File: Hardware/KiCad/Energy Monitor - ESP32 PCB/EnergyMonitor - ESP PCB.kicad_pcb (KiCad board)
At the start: 2 copper layers, 16 parts, among them J1 Conn_02x05_Odd_Even, J2 Conn_02x07_Odd_Even, J3 Conn_02x07_Odd_Even, J4 Conn_02x07_Odd_Even, J5 Conn_02x07_Odd_Even, J6 Conn_02x07_Odd_Even, J7 Conn_02x07_Odd_Even, U1 4072, U2 4072, U3 4072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

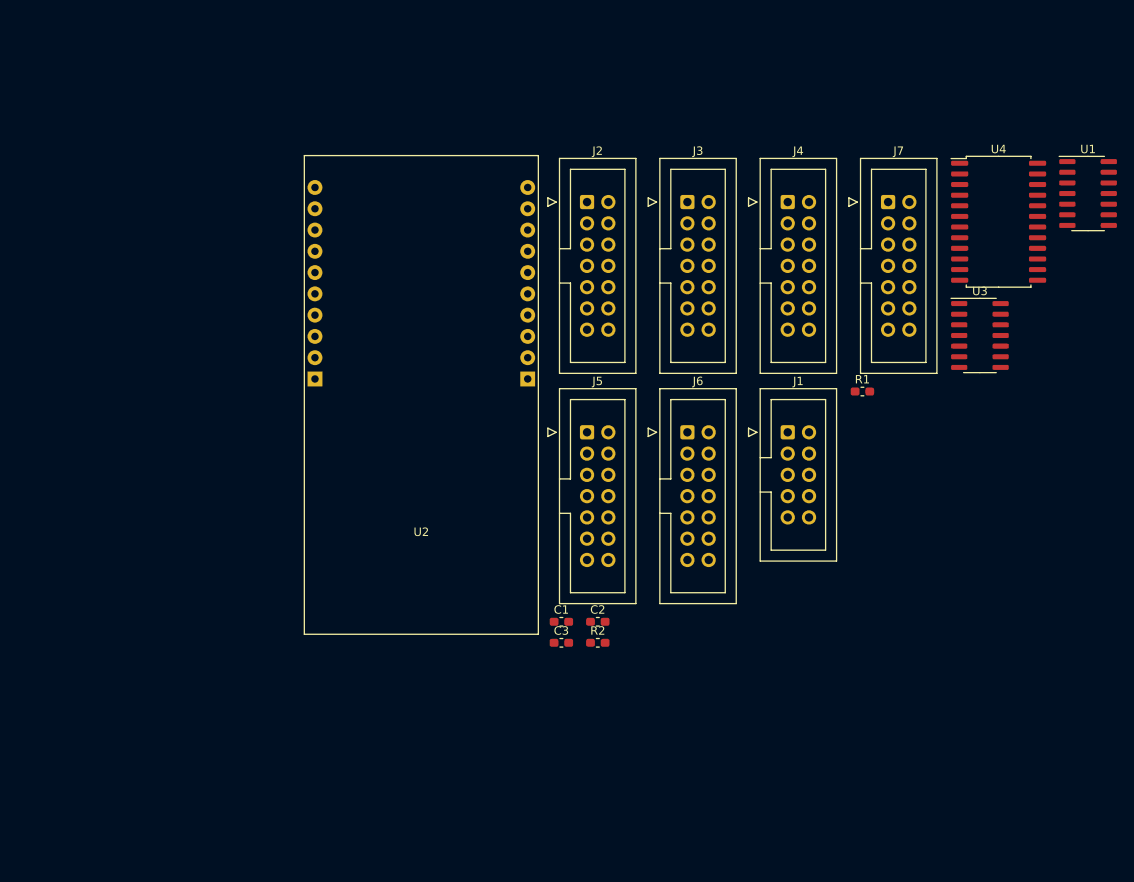
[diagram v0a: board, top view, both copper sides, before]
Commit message: This seems to be getting progressively more complicated. Library cleanup, moved everything to my system library.
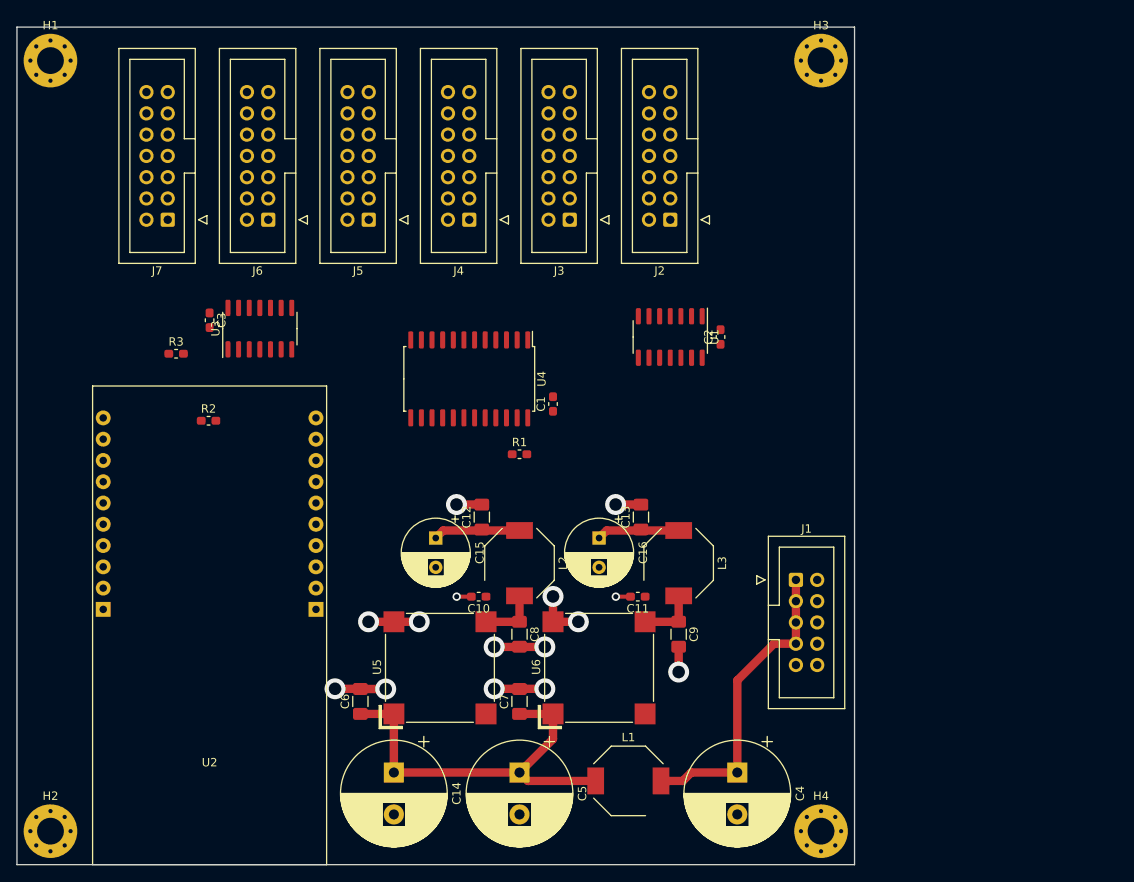
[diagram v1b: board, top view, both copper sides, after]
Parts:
- added C10: 0.1 uF, Capacitor_SMD:C_0603_1608Metric_Pad1.05x0.95mm_HandSolder, F.Cu at (95.1, 108.0)
- added C11: 0.1 uF, Capacitor_SMD:C_0603_1608Metric_Pad1.05x0.95mm_HandSolder, F.Cu at (114.1, 108.0)
- added C12: 22 uF, Capacitor_SMD:C_1206_3216Metric_Pad1.42x1.75mm_HandSolder, F.Cu at (95.5, 98.5)
- added C13: 22 uF, Capacitor_SMD:C_1206_3216Metric_Pad1.42x1.75mm_HandSolder, F.Cu at (114.5, 98.5)
- added C14: CP1, Capacitor_THT:CP_Radial_D12.5mm_P5.00mm, F.Cu at (85.0, 129.0)
- added C15: CP1, Capacitor_THT:CP_Radial_D8.0mm_P3.50mm, F.Cu at (90.0, 101.0)
- added C16: CP1, Capacitor_THT:CP_Radial_D8.0mm_P3.50mm, F.Cu at (109.5, 101.0)
- added C4: CP1, Capacitor_THT:CP_Radial_D12.5mm_P5.00mm, F.Cu at (126.0, 129.0)
- added C5: CP1, Capacitor_THT:CP_Radial_D12.5mm_P5.00mm, F.Cu at (100.0, 129.0)
- added C6: 10 uF, 35V, Capacitor_SMD:C_1206_3216Metric_Pad1.42x1.75mm_HandSolder, F.Cu at (81.0, 120.5)
- added C7: 10 uF, 35V, Capacitor_SMD:C_1206_3216Metric_Pad1.42x1.75mm_HandSolder, F.Cu at (100.0, 120.5)
- added C8: 22 uF, Capacitor_SMD:C_1206_3216Metric_Pad1.42x1.75mm_HandSolder, F.Cu at (100.0, 112.5)
- added C9: 22 uF, Capacitor_SMD:C_1206_3216Metric_Pad1.42x1.75mm_HandSolder, F.Cu at (119.0, 112.5)
- added H1: MountingHole, MountingHole:MountingHole_3.2mm_M3_Pad_Via, F.Cu at (44.0, 44.0)
- added H2: MountingHole, MountingHole:MountingHole_3.2mm_M3_Pad_Via, F.Cu at (44.0, 136.0)
- added H3: MountingHole, MountingHole:MountingHole_3.2mm_M3_Pad_Via, F.Cu at (136.0, 44.0)
- added H4: MountingHole, MountingHole:MountingHole_3.2mm_M3_Pad_Via, F.Cu at (136.0, 136.0)
- added L1: 47 uH, Inductor_SMD:L_Bourns-SRU8028_8.0x8.0mm, F.Cu at (113.0, 130.0)
- added L2: 47 uH, Inductor_SMD:L_Bourns-SRU8028_8.0x8.0mm, F.Cu at (100.0, 104.0)
- added L3: 47 uH, Inductor_SMD:L_Bourns-SRU8028_8.0x8.0mm, F.Cu at (119.0, 104.0)
- added R3: 330R, Resistor_SMD:R_0603_1608Metric_Pad1.05x0.95mm_HandSolder, F.Cu at (59.0, 79.0)
- added U5: VXO7805-500-M, custom:VXO78x-500-M, F.Cu at (90.5, 116.5)
- added U6: VXO7803-500-M, custom:VXO78x-500-M, F.Cu at (109.5, 116.5)
- U2: value 4072 -> ESP32-POE Module
- moved J7 86.0 mm to (58.0, 63.0), turned to 180 degrees
- moved U3 86.0 mm to (69.0, 76.0), turned to 90 degrees
- moved U4 65.9 mm to (94.0, 82.0), turned to 270 degrees
- moved C3 57.0 mm to (63.0, 75.0), turned to 270 degrees
- moved J6 56.1 mm to (70.0, 63.0), turned to 180 degrees
- moved R2 53.5 mm to (62.9, 87.0)
- moved U1 52.7 mm to (118.0, 77.0), turned to 270 degrees
- moved R1 41.6 mm to (100.0, 91.0)
- moved J4 38.1 mm to (94.0, 63.0), turned to 180 degrees
- moved U2 37.4 mm to (63.0, 140.0)
- moved C2 37.0 mm to (124.0, 77.0), turned to 90 degrees
- moved J5 36.4 mm to (82.0, 63.0), turned to 180 degrees
- moved C1 26.0 mm to (104.0, 85.0), turned to 90 degrees
- moved J1 17.6 mm to (133.0, 106.0)
- moved J3 14.2 mm to (106.0, 63.0), turned to 180 degrees
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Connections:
- J2 pad 2: +3V3 -> +5V
- J3 pad 2: +3V3 -> +5V
- J3 pad 4: /~CS_1 -> /~CS_3
- J3 pad 5: /IRQ_1 -> /IRQ_3
- J3 pad 6: /~CS_2 -> /~CS_4
- J3 pad 7: /IRQ_2 -> /IRQ_4
- J4 pad 2: +3V3 -> +5V
- J4 pad 4: Net-(J4-Pad4) -> /~CS_5
- J4 pad 5: /IRQ_1 -> /IRQ_5
- J4 pad 6: Net-(J4-Pad6) -> /~CS_6
- J4 pad 7: /IRQ_2 -> /IRQ_6
- J5 pad 2: +3V3 -> +5V
- J5 pad 4: /~CS_1 -> /~CS_7
- J5 pad 5: /IRQ_1 -> /IRQ_7
- J5 pad 6: /~CS_2 -> /~CS_8
- J5 pad 7: /IRQ_2 -> /IRQ_8
- J6 pad 2: +3V3 -> +5V
- J6 pad 4: /~CS_1 -> /~CS_9
- J6 pad 5: /IRQ_1 -> /IRQ_9
- J6 pad 6: /~CS_2 -> /~CS_10
- J6 pad 7: /IRQ_2 -> /IRQ_10
- J7 pad 2: +3V3 -> +5V
- J7 pad 4: /~CS_1 -> /~CS_11
- J7 pad 5: /IRQ_1 -> /IRQ_11
- J7 pad 6: /~CS_2 -> /~CS_12
- J7 pad 7: /IRQ_2 -> /IRQ_12
- U1 pad 10: /IRQ_1 -> /IRQ_5
- U1 pad 11: /IRQ_2 -> /IRQ_4
- U1 pad 12: /IRQ_1 -> /IRQ_3
- U1 pad 3: /IRQ_2 -> Net-(U1-Pad13)
- U1 pad 4: /IRQ_1 -> /IRQ_2
- U1 pad 5: Net-(U1-Pad5) -> /IRQ_1
- U1 pad 9: /IRQ_2 -> /IRQ_6
- U2 pad 1: Net-(U2-Pad1) -> +5V
- U2 pad 11: Net-(R2-Pad1) -> Net-(R3-Pad1)
- U2 pad 12: Net-(U2-Pad12) -> Net-(R2-Pad1)
- U2 pad 2: +3V3 -> Net-(U2-Pad2)
- U3 pad 1: Net-(U1-Pad5) -> Net-(R3-Pad2)
- U3 pad 10: /IRQ_1 -> /IRQ_11
- U3 pad 11: /IRQ_2 -> /IRQ_10
- U3 pad 12: /IRQ_1 -> /IRQ_9
- U3 pad 4: /IRQ_2 -> /IRQ_8
- U3 pad 5: /IRQ_1 -> /IRQ_7
- U3 pad 9: /IRQ_2 -> /IRQ_12
- U4 pad 10: /~CS_2 -> /~CS_10
- U4 pad 11: /~CS_1 -> /~CS_11
- U4 pad 13: /~CS_2 -> /~CS_12
- U4 pad 3: /~CS_1 -> /~CS_3
- U4 pad 4: /~CS_2 -> /~CS_4
- U4 pad 5: Net-(U4-Pad5) -> /~CS_5
- U4 pad 6: Net-(U4-Pad6) -> /~CS_6
- U4 pad 7: /~CS_1 -> /~CS_7
- U4 pad 8: /~CS_2 -> /~CS_8
- U4 pad 9: /~CS_1 -> /~CS_9
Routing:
- net Net-(C14-Pad1): track 0.00 -> 48.2 mm
- net GND: track 0.00 -> 42.8 mm, vias 0 -> 15
- net +9V: track 0.00 -> 36.9 mm
- net +5V: track 0.00 -> 10.4 mm
- net +3V3: track 0.00 -> 9.87 mm
- net Net-(C11-Pad1): track 0.00 -> 7.10 mm
- net Net-(C10-Pad1): track 0.00 -> 7.10 mm
- added copper zone on In2.Cu, net +3V3
- added copper zone on In1.Cu, net GND
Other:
- board outline added: 100 x 100 mm
- copper layers 2 -> 4

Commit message: Updates! I keep adding features.
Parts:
- removed C1, C10, C11, C2, C3: 0.1 uF, Capacitor_SMD:C_0603_1608Metric_Pad1.05x0.95mm_HandSolder
- removed C12, C13, C8, C9: 22 uF, Capacitor_SMD:C_1206_3216Metric_Pad1.42x1.75mm_HandSolder
- removed C14, C4, C5: CP1, Capacitor_THT:CP_Radial_D12.5mm_P5.00mm
- removed C15, C16: CP1, Capacitor_THT:CP_Radial_D8.0mm_P3.50mm
- removed C6, C7: 10 uF, 35V, Capacitor_SMD:C_1206_3216Metric_Pad1.42x1.75mm_HandSolder
- removed H1, H2, H3, H4: MountingHole, MountingHole:MountingHole_3.2mm_M3_Pad_Via
- removed J1: Conn_02x05_Odd_Even, Connector_IDC:IDC-Header_2x05_P2.54mm_Vertical
- removed J2, J3, J4, J5, J6, J7: Conn_02x07_Odd_Even, Connector_IDC:IDC-Header_2x07_P2.54mm_Vertical
- removed L1, L2, L3: 47 uH, Inductor_SMD:L_Bourns-SRU8028_8.0x8.0mm
- removed R1: 10K, Resistor_SMD:R_0603_1608Metric_Pad1.05x0.95mm_HandSolder
- removed R2, R3: 330R, Resistor_SMD:R_0603_1608Metric_Pad1.05x0.95mm_HandSolder
- removed U1, U3: 4072, Package_SO:SOIC-14_3.9x8.7mm_P1.27mm
- removed U2: ESP32-POE Module, Energy Monitor - ESP32 PCB:ESP32-POE
- removed U4: 4072, Package_SO:SOIC-24W_7.5x15.4mm_P1.27mm
- removed U5: VXO7805-500-M, custom:VXO78x-500-M
- removed U6: VXO7803-500-M, custom:VXO78x-500-M
- added J10: Conn_01x04, Connector_PinHeader_2.54mm:PinHeader_1x04_P2.54mm_Vertical, F.Cu at (134.0, 85.7)
- added J8: Conn_01x04, Connector_PinHeader_2.54mm:PinHeader_1x04_P2.54mm_Vertical, F.Cu at (118.7, 85.7)
- added J9: Conn_01x04, Connector_PinHeader_2.54mm:PinHeader_1x04_P2.54mm_Vertical, F.Cu at (126.4, 85.7)
- added LCD?1: 0.96, custom:12864-DISP-I2C, F.Cu at (124.0, 52.0)
- added R4: 2.2K, Resistor_SMD:R_0603_1608Metric_Pad1.05x0.95mm_HandSolder, F.Cu at (73.0, 98.5)
- added R5: 2.2K, Resistor_SMD:R_0603_1608Metric_Pad1.05x0.95mm_HandSolder, F.Cu at (73.0, 95.0)
- added R6: 10K, Resistor_SMD:R_0603_1608Metric_Pad1.05x0.95mm_HandSolder, F.Cu at (114.0, 89.5)
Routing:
- net +5V: track 10.4 -> 150.5 mm
- net /ESP1/MISO: track 0.00 -> 126.3 mm
- net /ESP1/MOSI: track 0.00 -> 114.5 mm, vias 0 -> 1
- net /ESP1/SCLK: track 0.00 -> 101.0 mm
- net /ESP1/IRQ_7: track 0.00 -> 55.7 mm
- net /ESP1/IRQ_8: track 0.00 -> 52.8 mm
- net /ESP1/IRQ_9: track 0.00 -> 44.9 mm
- net /ESP1/IRQ_10: track 0.00 -> 38.8 mm
- net /ESP1/IRQ_11: track 0.00 -> 32.2 mm
- net /ESP1/IRQ_12: track 0.00 -> 30.9 mm
- net +3V3: track 9.87 -> 40.6 mm, vias 0 -> 6
- net Net-(R2-Pad1): track 0.00 -> 30.5 mm
- net Net-(R1-Pad2): track 0.00 -> 25.5 mm
- net Net-(U2-Pad20): track 0.00 -> 24.5 mm
- net Net-(U2-Pad16): track 0.00 -> 23.5 mm
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
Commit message: Progress!
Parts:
- added J11: Conn_01x05, Connector_PinHeader_2.54mm:PinHeader_1x05_P2.54mm_Vertical, F.Cu at (117.5, 43.0)
- added J12: Conn_01x05, Connector_PinHeader_2.54mm:PinHeader_1x05_P2.54mm_Vertical, F.Cu at (117.5, 48.0)
- moved LCD1 1.50 mm to (124.0, 53.5)
- renumbered LCD?1 to LCD1
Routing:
- net +5V: track 150.5 -> 0.00 mm
- net /ESP1/MISO: track 126.3 -> 0.00 mm
- net /ESP1/MOSI: track 114.5 -> 0.00 mm, vias 1 -> 0
- net /ESP1/SCLK: track 101.0 -> 0.00 mm
- net /ESP1/IRQ_7: track 55.7 -> 0.00 mm
- net /ESP1/IRQ_8: track 52.8 -> 0.00 mm
- net GND: track 50.3 -> 0.00 mm, vias 21 -> 0
- net Net-(C14-Pad1): track 48.2 -> 0.00 mm
- net /ESP1/IRQ_9: track 44.9 -> 0.00 mm
- net +3V3: track 40.6 -> 0.00 mm, vias 6 -> 0
- net /ESP1/IRQ_10: track 38.8 -> 0.00 mm
- net +9V: track 36.9 -> 0.00 mm
- net /ESP1/IRQ_11: track 32.2 -> 0.00 mm
- net /ESP1/IRQ_12: track 30.9 -> 0.00 mm
- net Net-(R2-Pad1): track 30.5 -> 0.00 mm
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- removed copper zone on In2.Cu, net +3V3
- removed copper zone on In1.Cu, net GND
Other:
- board outline removed
